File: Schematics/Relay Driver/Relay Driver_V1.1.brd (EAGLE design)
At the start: 76.2 x 50.8 mm, 19 parts, among them IC1 74AC04N

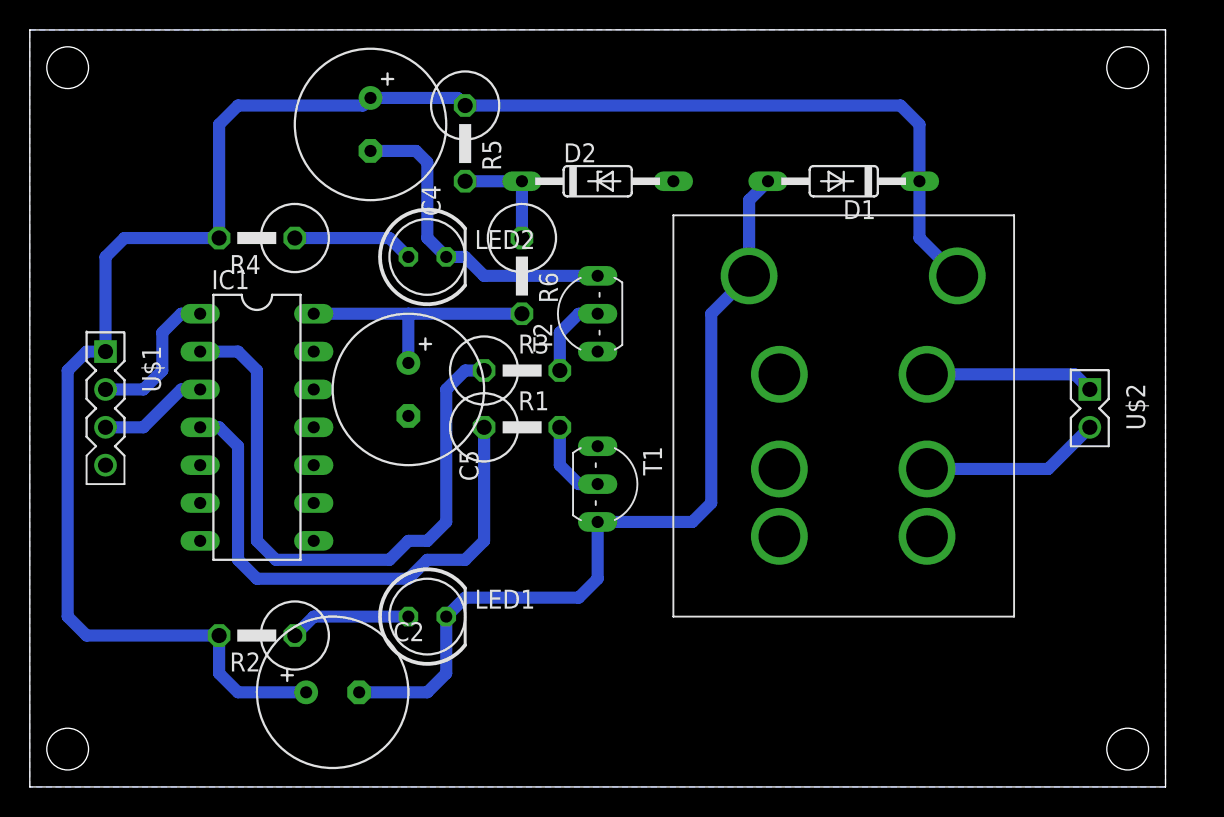
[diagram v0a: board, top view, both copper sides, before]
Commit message: Updated relay board, updated documentation
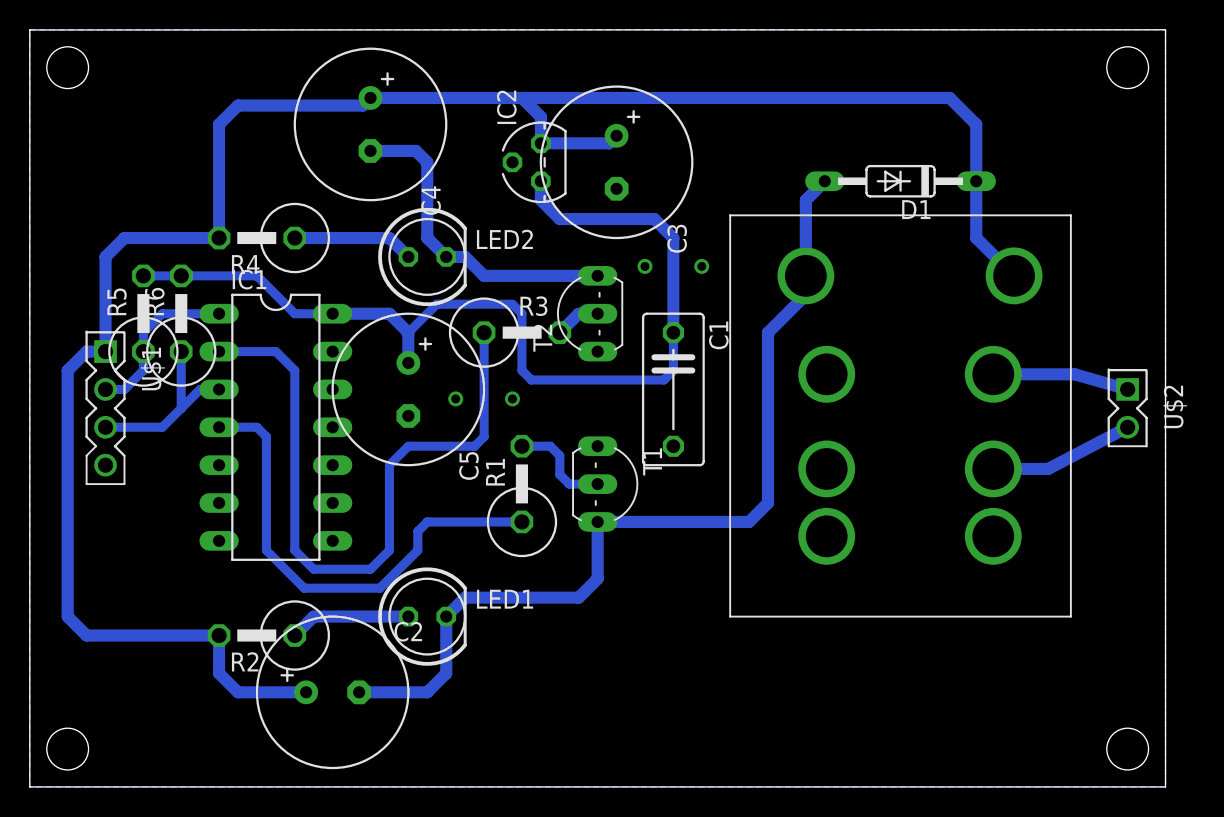
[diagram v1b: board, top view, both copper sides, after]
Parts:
- removed D2: 5.1V, diode:DO35Z10
- added C1: 10nF, rcl:C075-042X103
- added C3: .33uF, rcl:E3,5-10
- added IC2: 7805L, linear:TO92
- moved R5 24.4 mm to (7.62, 31.8), turned to 90 degrees
- moved R6 23.0 mm to (10.2, 31.8), turned to 90 degrees
- moved D1 3.81 mm to (58.4, 40.6)
- moved RL1 3.81 mm to (52.1, 34.3)
- moved R1 3.81 mm to (33.0, 20.3), turned to 90 degrees
- moved R3 2.54 mm to (33.0, 30.5)
- moved U$2 2.54 mm to (73.7, 24.1)
- moved IC1 1.27 mm to (16.5, 24.1)
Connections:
- removed net N$12: C5.+, IC1.14, R6.2
- removed net N$13: D2.C, R5.2, R6.1
- new net +5V: C1.1, C5.+, IC1.14, IC2.1, R5.2, R6.2
- net +8V: now also C3.+, IC2.3; no longer R5.1
- net GND: now also C1.2, C3.-, IC2.2; no longer D2.A
- net N$6: now also R5.1
- net N$8: now also R6.1
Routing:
- net +5V: track 0.00 -> 64.7 mm
- net N$12: track 17.3 -> 0.00 mm
- net +8V: track 121.0 -> 133.6 mm
- net N$13: track 7.62 -> 0.00 mm
- net N$8: track 7.40 -> 12.5 mm
- net G1: track 36.4 -> 31.8 mm
- net N$4: track 56.5 -> 60.3 mm
- net G0: track 42.0 -> 44.9 mm
- net N$3: track 5.61 -> 3.07 mm
- net N$2: track 12.1 -> 9.70 mm
- net N$5: track 11.3 -> 9.16 mm
- net N$6: track 9.94 -> 11.2 mm
- net N$1: track 5.61 -> 6.88 mm
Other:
- board text added: "Add Jumper"
